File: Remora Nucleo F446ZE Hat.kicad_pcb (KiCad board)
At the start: 2 copper layers, 70 x 133.3 mm, 75 parts, among them J1 NucleoF446ZE CN11 Header, J2 NucleoF446ZE CN12 Header, U10 HT26LS31ARZ, U11 ADuM1201AR, U12 ADuM1201AR, U13 HT26LS31ARZ, U14 ADuM1201AR, U15 ADuM1201AR, U16 ADuM1201AR, U17 ADuM1201AR, U18 ADuM1201AR, U19 ADuM1201AR, U2 TPS5430DDAR, U3 TPS5430DDAR, U4 TPS5430DDAR, U5 ADuM1201AR, U6 ADuM1201AR, U7 ADuM1201AR, U8 ADuM1201AR, U9 HT26LS31ARZ

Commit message: Deleted stale test production files. Fixed up a bug with power isolation. Created some footprints for wire to board connectors although ran out of time to fix a bug where they do no lock in. Fixes to readme
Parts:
- added C10: 100nF, Capacitor_SMD:C_1206_3216Metric_Pad1.33x1.80mm_HandSolder, F.Cu at (-78.6, 41.0)
- added C11: 100nF, Capacitor_SMD:C_1206_3216Metric_Pad1.33x1.80mm_HandSolder, F.Cu at (-78.6, 44.3)
- added C12: 100nF, Capacitor_SMD:C_1206_3216Metric_Pad1.33x1.80mm_HandSolder, F.Cu at (-78.6, 47.7)
- added C13: 100nF, Capacitor_SMD:C_1206_3216Metric_Pad1.33x1.80mm_HandSolder, F.Cu at (-78.6, 51.0)
- added C14: 100nF, Capacitor_SMD:C_1206_3216Metric_Pad1.33x1.80mm_HandSolder, F.Cu at (-95.0, 56.1)
- added C15: 100nF, Capacitor_SMD:C_1206_3216Metric_Pad1.33x1.80mm_HandSolder, F.Cu at (-95.0, 59.5)
- added C16: 100nF, Capacitor_SMD:C_1206_3216Metric_Pad1.33x1.80mm_HandSolder, F.Cu at (-95.0, 62.9)
- added C17: 100nF, Capacitor_SMD:C_1206_3216Metric_Pad1.33x1.80mm_HandSolder, F.Cu at (-95.0, 66.2)
- added C18: 100nF, Capacitor_SMD:C_1206_3216Metric_Pad1.33x1.80mm_HandSolder, F.Cu at (-95.0, 24.7)
- added C19: 100nF, Capacitor_SMD:C_1206_3216Metric_Pad1.33x1.80mm_HandSolder, F.Cu at (-95.0, 28.0)
- added C20: 100nF, Capacitor_SMD:C_1206_3216Metric_Pad1.33x1.80mm_HandSolder, F.Cu at (-95.0, 31.4)
- added C21: 100nF, Capacitor_SMD:C_1206_3216Metric_Pad1.33x1.80mm_HandSolder, F.Cu at (-95.0, 34.7)
- added C22: 100nF, Capacitor_SMD:C_1206_3216Metric_Pad1.33x1.80mm_HandSolder, F.Cu at (-67.7, 32.8)
- added C24: 100nF, Capacitor_SMD:C_1206_3216Metric_Pad1.33x1.80mm_HandSolder, F.Cu at (-112.3, 19.3)
- added C25: 100nF, Capacitor_SMD:C_1206_3216Metric_Pad1.33x1.80mm_HandSolder, F.Cu at (-57.4, 91.9)
- added C26: 100nF, Capacitor_SMD:C_1206_3216Metric_Pad1.33x1.80mm_HandSolder, F.Cu at (-57.4, 95.2)
- added C27: 100nF, Capacitor_SMD:C_1206_3216Metric_Pad1.33x1.80mm_HandSolder, F.Cu at (-36.5, 91.9)
- added C28: 100nF, Capacitor_SMD:C_1206_3216Metric_Pad1.33x1.80mm_HandSolder, F.Cu at (-36.5, 95.2)
- added C29: 100nF, Capacitor_SMD:C_1206_3216Metric_Pad1.33x1.80mm_HandSolder, F.Cu at (-29.5, 44.8)
- added C30: 100nF, Capacitor_SMD:C_1206_3216Metric_Pad1.33x1.80mm_HandSolder, F.Cu at (-29.5, 48.1)
- added C31: 100nF, Capacitor_SMD:C_1206_3216Metric_Pad1.33x1.80mm_HandSolder, F.Cu at (-26.1, 76.6)
- added C32: 100nF, Capacitor_SMD:C_1206_3216Metric_Pad1.33x1.80mm_HandSolder, F.Cu at (-26.1, 79.9)
- added C33: 100nF, Capacitor_SMD:C_1206_3216Metric_Pad1.33x1.80mm_HandSolder, F.Cu at (-72.2, 103.8)
- added C34: 100nF, Capacitor_SMD:C_1206_3216Metric_Pad1.33x1.80mm_HandSolder, F.Cu at (-72.2, 107.2)
- added C35: 100nF, Capacitor_SMD:C_1206_3216Metric_Pad1.33x1.80mm_HandSolder, F.Cu at (-57.4, 107.2)
- added C36: 100nF, Capacitor_SMD:C_1206_3216Metric_Pad1.33x1.80mm_HandSolder, F.Cu at (-57.4, 110.5)
- added C37: 100nF, Capacitor_SMD:C_1206_3216Metric_Pad1.33x1.80mm_HandSolder, F.Cu at (-47.0, 107.2)
- added C38: 100nF, Capacitor_SMD:C_1206_3216Metric_Pad1.33x1.80mm_HandSolder, F.Cu at (-47.0, 110.5)
- added C39: 100nF, Capacitor_SMD:C_1206_3216Metric_Pad1.33x1.80mm_HandSolder, F.Cu at (-47.0, 76.6)
- added C40: 100nF, Capacitor_SMD:C_1206_3216Metric_Pad1.33x1.80mm_HandSolder, F.Cu at (-47.0, 79.9)
- added C41: 100nF, Capacitor_SMD:C_1206_3216Metric_Pad1.33x1.80mm_HandSolder, F.Cu at (-26.1, 107.2)
- added C42: 100nF, Capacitor_SMD:C_1206_3216Metric_Pad1.33x1.80mm_HandSolder, F.Cu at (-26.1, 110.5)
- added C43: 100nF, Capacitor_SMD:C_1206_3216Metric_Pad1.33x1.80mm_HandSolder, F.Cu at (-47.0, 91.9)
- added C44: 100nF, Capacitor_SMD:C_1206_3216Metric_Pad1.33x1.80mm_HandSolder, F.Cu at (-47.0, 95.2)
- added C45: 100nF, Capacitor_SMD:C_1206_3216Metric_Pad1.33x1.80mm_HandSolder, F.Cu at (-36.5, 107.2)
- added C46: 100nF, Capacitor_SMD:C_1206_3216Metric_Pad1.33x1.80mm_HandSolder, F.Cu at (-36.5, 110.5)
- added C47: 100nF, Capacitor_SMD:C_1206_3216Metric_Pad1.33x1.80mm_HandSolder, F.Cu at (-26.1, 91.9)
- added C48: 100nF, Capacitor_SMD:C_1206_3216Metric_Pad1.33x1.80mm_HandSolder, F.Cu at (-26.1, 95.2)
- added C49: 100nF, Capacitor_SMD:C_1206_3216Metric_Pad1.33x1.80mm_HandSolder, F.Cu at (-36.5, 76.6)
- added C50: 100nF, Capacitor_SMD:C_1206_3216Metric_Pad1.33x1.80mm_HandSolder, F.Cu at (-36.5, 79.9)
- added C51: 100nF, Capacitor_SMD:C_1206_3216Metric_Pad1.33x1.80mm_HandSolder, F.Cu at (-57.4, 76.6)
- added C52: 100nF, Capacitor_SMD:C_1206_3216Metric_Pad1.33x1.80mm_HandSolder, F.Cu at (-57.4, 79.9)
- added D8: 3V3LED, Diode_SMD:D_1206_3216Metric_Pad1.42x1.75mm_HandSolder, F.Cu at (-33.2, 24.7)
- added F1: 45mA Resettable Fuse (PRG18BB101MB1RB), Fuse:Fuse_0603_1608Metric_Pad1.05x0.95mm_HandSolder, F.Cu at (-79.4, 96.8)
- added F10: 45mA Resettable Fuse (PRG18BB101MB1RB), Fuse:Fuse_0603_1608Metric_Pad1.05x0.95mm_HandSolder, F.Cu at (-79.4, 69.6)
- added F2: 45mA Resettable Fuse (PRG18BB101MB1RB), Fuse:Fuse_0603_1608Metric_Pad1.05x0.95mm_HandSolder, F.Cu at (-79.4, 56.0)
- added F3: 45mA Resettable Fuse (PRG18BB101MB1RB), Fuse:Fuse_0603_1608Metric_Pad1.05x0.95mm_HandSolder, F.Cu at (-64.6, 56.0)
- added F4: 45mA Resettable Fuse (PRG18BB101MB1RB), Fuse:Fuse_0603_1608Metric_Pad1.05x0.95mm_HandSolder, F.Cu at (-35.0, 56.0)
- added F5: 45mA Resettable Fuse (PRG18BB101MB1RB), Fuse:Fuse_0603_1608Metric_Pad1.05x0.95mm_HandSolder, F.Cu at (-64.6, 83.2)
- added F6: 45mA Resettable Fuse (PRG18BB101MB1RB), Fuse:Fuse_0603_1608Metric_Pad1.05x0.95mm_HandSolder, F.Cu at (-79.4, 83.2)
- added F7: 45mA Resettable Fuse (PRG18BB101MB1RB), Fuse:Fuse_0603_1608Metric_Pad1.05x0.95mm_HandSolder, F.Cu at (-49.8, 56.0)
- added F8: 45mA Resettable Fuse (PRG18BB101MB1RB), Fuse:Fuse_0603_1608Metric_Pad1.05x0.95mm_HandSolder, F.Cu at (-36.7, 37.8)
- added F9: 45mA Resettable Fuse (PRG18BB101MB1RB), Fuse:Fuse_0603_1608Metric_Pad1.05x0.95mm_HandSolder, F.Cu at (-64.6, 69.6)
- added J10: B_STEP_AND_DIR+-, OSTVTerminalBlocks:Conn01x06, F.Cu at (-106.7, 27.1)
- added J11: C_STEP_AND_DIR+-, OSTVTerminalBlocks:Conn01x06, F.Cu at (-106.7, 35.2)
- added J12: DIGITAL_OUTPUTS, OSTVTerminalBlocks:Conn01x12, F.Cu at (-54.4, 27.1)
- added J13: 0-10V Spindle Out, OSTVTerminalBlocks:Conn01x02, F.Cu at (-27.2, 58.8)
- added J14: Digital Inputs, OSTVTerminalBlocks:Conn01x30, F.Cu at (-76.2, 13.6)
- added J3: 5V_SUPPLY, OSTVTerminalBlocks:Conn01x02, F.Cu at (-67.1, 40.6)
- added J4: 5V_AUXOUT, OSTVTerminalBlocks:Conn01x02, F.Cu at (-60.0, 40.6)
- added J5: 24V Power Inlet, OSTVTerminalBlocks:Conn01x02, F.Cu at (-52.9, 40.6)
- added J6: X_STEP_AND_DIR+-, OSTVTerminalBlocks:Conn01x06, F.Cu at (-81.4, 27.1)
- added J7: Y_STEP_AND_DIR+-, OSTVTerminalBlocks:Conn01x06, F.Cu at (-81.4, 35.2)
- added J8: Z_STEP_AND_DIR+-, OSTVTerminalBlocks:Conn01x06, F.Cu at (-106.7, 58.6)
- added J9: A_STEP_AND_DIR+-, OSTVTerminalBlocks:Conn01x06, F.Cu at (-106.7, 66.7)
- added JP1: EXT_5V_SUPPLY_JMP, Jumper:SolderJumper-2_P1.3mm_Open_TrianglePad1.0x1.5mm, F.Cu at (-68.5, 46.4)
- added JP2: EXT_5V_GND_JMP, Jumper:SolderJumper-2_P1.3mm_Open_TrianglePad1.0x1.5mm, F.Cu at (-68.5, 50.0)
- added R17: 100R, Resistor_SMD:R_1206_3216Metric_Pad1.30x1.75mm_HandSolder, F.Cu at (-33.2, 28.0)
- added U10: LTV-817S, Package_SO:SOIC-16_3.9x9.9mm_P1.27mm, F.Cu at (-71.0, 60.6)
- added U11: LTV-817S, Package_SO:SOIC-16_3.9x9.9mm_P1.27mm, F.Cu at (-41.4, 60.6)
- added U12: LTV-817S, Package_SO:SOIC-16_3.9x9.9mm_P1.27mm, F.Cu at (-71.0, 87.8)
- added U13: LTV-817S, Package_SO:SOIC-16_3.9x9.9mm_P1.27mm, F.Cu at (-85.8, 87.8)
- added U14: ADuM1200AR, Package_SO:SOIC-8_3.9x4.9mm_P1.27mm, F.Cu at (-111.1, 74.2)
- added U15: ADuM1200AR, Package_SO:SOIC-8_3.9x4.9mm_P1.27mm, F.Cu at (-111.1, 80.7)
- added U16: HT26LS31ARZ, Package_DIP:SMDIP-4_W9.53mm, F.Cu at (-100.3, 74.1)
- added U17: ADuM1200AR, Package_SO:SOIC-8_3.9x4.9mm_P1.27mm, F.Cu at (-111.1, 42.7)
- added U18: ADuM1200AR, Package_SO:SOIC-8_3.9x4.9mm_P1.27mm, F.Cu at (-111.1, 49.2)
- added U19: HT26LS31ARZ, Package_DIP:SMDIP-4_W9.53mm, F.Cu at (-100.3, 42.6)
- added U20: LTV-817S, Package_SO:SOIC-16_3.9x9.9mm_P1.27mm, F.Cu at (-56.2, 60.6)
- added U21: LTV-817S, Package_SO:SOIC-16_3.9x9.9mm_P1.27mm, F.Cu at (-43.1, 42.4)
- added U22: LTV-817S, Package_SO:SOIC-16_3.9x9.9mm_P1.27mm, F.Cu at (-71.0, 74.2)
- added U23: LTV-817S, Package_SO:SOIC-16_3.9x9.9mm_P1.27mm, F.Cu at (-85.8, 74.2)
- added U26: ADuM1200AR, Package_SO:SOIC-8_3.9x4.9mm_P1.27mm, F.Cu at (-56.2, 87.0)
- added U27: ADuM1200AR, Package_SO:SOIC-8_3.9x4.9mm_P1.27mm, F.Cu at (-35.3, 87.0)
- added U28: ADuM1200AR, Package_SO:SOIC-8_3.9x4.9mm_P1.27mm, F.Cu at (-28.3, 39.9)
- added U29: ADuM1200AR, Package_SO:SOIC-8_3.9x4.9mm_P1.27mm, F.Cu at (-24.8, 71.7)
- added U30: ADuM1200AR, Package_SO:SOIC-8_3.9x4.9mm_P1.27mm, F.Cu at (-71.0, 98.9)
- added U31: ADuM1200AR, Package_SO:SOIC-8_3.9x4.9mm_P1.27mm, F.Cu at (-56.2, 102.2)
- added U32: ADuM1200AR, Package_SO:SOIC-8_3.9x4.9mm_P1.27mm, F.Cu at (-45.7, 102.2)
- added U33: ADuM1200AR, Package_SO:SOIC-8_3.9x4.9mm_P1.27mm, F.Cu at (-45.7, 71.7)
- added U34: ADuM1200AR, Package_SO:SOIC-8_3.9x4.9mm_P1.27mm, F.Cu at (-24.8, 102.2)
- added U35: ADuM1200AR, Package_SO:SOIC-8_3.9x4.9mm_P1.27mm, F.Cu at (-45.7, 87.0)
- added U36: ADuM1200AR, Package_SO:SOIC-8_3.9x4.9mm_P1.27mm, F.Cu at (-35.3, 102.2)
- added U37: ADuM1200AR, Package_SO:SOIC-8_3.9x4.9mm_P1.27mm, F.Cu at (-24.8, 87.0)
- added U38: ADuM1200AR, Package_SO:SOIC-8_3.9x4.9mm_P1.27mm, F.Cu at (-35.3, 71.7)
- added U39: ADuM1200AR, Package_SO:SOIC-8_3.9x4.9mm_P1.27mm, F.Cu at (-56.2, 71.7)
- added U5: ADuM1200AR, Package_SO:SOIC-8_3.9x4.9mm_P1.27mm, F.Cu at (-85.8, 42.7)
- added U6: ADuM1200AR, Package_SO:SOIC-8_3.9x4.9mm_P1.27mm, F.Cu at (-85.8, 49.2)
- added U8: LTV-817S, Package_SO:SOIC-16_3.9x9.9mm_P1.27mm, F.Cu at (-85.8, 101.5)
- added U9: LTV-817S, Package_SO:SOIC-16_3.9x9.9mm_P1.27mm, F.Cu at (-85.8, 60.6)
- U7: renamed from U9; footprint Package_SO:SOIC-16_3.9x9.9mm_P1.27mm -> Package_DIP:SMDIP-4_W9.53mm
- moved U10 271.7 mm to (-74.5, 135.5)
- moved U11 271.7 mm to (-83.5, 146.1)
- moved U12 271.7 mm to (-83.5, 152.7)
- moved U13 271.7 mm to (-74.4, 148.9)
- moved U5 271.7 mm to (-83.5, 119.8)
- moved U6 271.7 mm to (-83.5, 126.4)
- moved U7 271.7 mm to (-83.5, 133.0)
- moved U8 271.7 mm to (-83.5, 139.6)
- moved U7 271.7 mm to (-74.3, 122.4)
- moved C1 179.9 mm to (-101.0, 96.6)
- moved C10 179.9 mm to (-100.9, 125.0)
- moved C11 179.9 mm to (-112.9, 125.0)
- moved C12 179.9 mm to (-100.9, 128.3)
- moved C13 179.9 mm to (-112.9, 131.7)
- moved C14 179.9 mm to (-112.9, 121.7)
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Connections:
- net /Regulators/12V_SENSE renamed /Regulators and Power Management/12V_SENSE
- net /Regulators/3V3_SENSE renamed /Regulators and Power Management/3V3_SENSE
- net /Regulators/5V_SENSE renamed /Regulators and Power Management/5V_SENSE
- J1 pad 14: unconnected-(J1-Pin_14-Pad14) -> MCU_RST
- J1 pad 23: unconnected-(J1-Pin_23-Pad23) -> USR_BTN
- J2 pad 28: unconnected-(J2-Pin_28-Pad28) -> USR_LED
- U7 pad 2: /Stepper_drivers/X_STEP+ -> /X and Y Stepper Drivers/X_STEP+
- U7 pad 3: /Stepper_drivers/X_STEP- -> /X and Y Stepper Drivers/X_STEP-

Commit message: Fixes to screw terminal footprints, updated BOM and included in project folder
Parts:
- added J15: 24V Peripheral, EBWA_02_A:ADAMTECH_EBWA-02-A, F.Cu at (-94.8, 4.50)
- added U40: LTV-817S, Package_SO:SOIC-16_3.9x9.9mm_P1.27mm, F.Cu at (-95.2, -7.75)
- added U42: TL431DBZ, Package_TO_SOT_SMD:SOT-23, F.Cu at (-88.5, -11.2)
- J10, J11, J6, J7, J8, J9: footprint OSTVTerminalBlocks:Conn01x06 -> EBWA_06_A:CONN_EBWA-06-A_ADM
- J12: footprint OSTVTerminalBlocks:Conn01x12 -> EBWA_06_A:CONN_EBWA-12-A_ADM
- J13: value 0-10V Spindle Out -> Spindle Out; footprint OSTVTerminalBlocks:Conn01x02 -> EBWA_02_A:ADAMTECH_EBWA-02-A
- J14: footprint OSTVTerminalBlocks:Conn01x30 -> EBWA_06_A:CONN_EBWA-30-A_ADM
- J5: value 24V Power Inlet -> 24V Logic; footprint OSTVTerminalBlocks:Conn01x02 -> EBWA_02_A:ADAMTECH_EBWA-02-A
- moved J10 192.3 mm to (79.5, -21.0)
- moved J11 192.3 mm to (79.5, -12.8)
- moved J12 192.3 mm to (131.8, -21.0)
- moved J14 192.3 mm to (110.0, -34.5)
- moved J6 192.3 mm to (104.8, -21.0)
- moved J7 192.3 mm to (104.8, -12.8)
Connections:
- C1 pad 1: +12V -> VDD
- C12 pad 2: 5V_GND -> GNDPWR
- C13 pad 2: 5V_GND -> GNDPWR
- C16 pad 2: 5V_GND -> GNDPWR
- C17 pad 2: 5V_GND -> GNDPWR
- C20 pad 2: 5V_GND -> GNDPWR
- C21 pad 2: 5V_GND -> GNDPWR
- C22 pad 2: 5V_GND -> GNDPWR
- C24 pad 2: 5V_GND -> GNDPWR
- C25 pad 2: 5V_GND -> GNDPWR
- C27 pad 2: 5V_GND -> GNDPWR
- C29 pad 2: 5V_GND -> GNDPWR
- C31 pad 2: 5V_GND -> GNDPWR
- C33 pad 2: 5V_GND -> GNDPWR
- C35 pad 2: 5V_GND -> GNDPWR
- C37 pad 2: 5V_GND -> GNDPWR
- C39 pad 2: 5V_GND -> GNDPWR
- C41 pad 2: 5V_GND -> GNDPWR
- C43 pad 2: 5V_GND -> GNDPWR
- C45 pad 2: 5V_GND -> GNDPWR
- C47 pad 2: 5V_GND -> GNDPWR
- C49 pad 2: 5V_GND -> GNDPWR
- C51 pad 2: 5V_GND -> GNDPWR
- C6 pad 1: +12V -> +24V
- D6 pad 1: GNDREF -> GNDPWR
- J10 pad 6: 5V_GND -> GNDPWR
- J11 pad 6: 5V_GND -> GNDPWR
- J12 pad 12: 5V_GND -> GNDPWR
- J13 pad 2: GNDREF -> GNDPWR
- J14 pad 30: 5V_GND -> GNDPWR
- J6 pad 6: 5V_GND -> GNDPWR
- J7 pad 6: 5V_GND -> GNDPWR
- J8 pad 6: 5V_GND -> GNDPWR
- J9 pad 6: 5V_GND -> GNDPWR
- R2 pad 1: +5V -> +5VD
- R3 pad 2: GNDREF -> GNDPWR
- U1 pad 6: +5V -> +5VD
- U10 pad 3: 5V_GND -> GNDPWR
- U11 pad 3: 5V_GND -> GNDPWR
- U12 pad 3: 5V_GND -> GNDPWR
- U13 pad 3: 5V_GND -> GNDPWR
- U14 pad 5: 5V_GND -> GNDPWR
- U15 pad 5: 5V_GND -> GNDPWR
- U17 pad 5: 5V_GND -> GNDPWR
- U18 pad 5: 5V_GND -> GNDPWR
- U2 pad 7: +12V -> VDD
- U20 pad 3: 5V_GND -> GNDPWR
- U21 pad 3: 5V_GND -> GNDPWR
- U22 pad 3: 5V_GND -> GNDPWR
- U23 pad 3: 5V_GND -> GNDPWR
- U26 pad 4: 5V_GND -> GNDPWR
- U27 pad 4: 5V_GND -> GNDPWR
- U28 pad 4: 5V_GND -> GNDPWR
- U29 pad 4: 5V_GND -> GNDPWR
- U30 pad 4: 5V_GND -> GNDPWR
- U31 pad 4: 5V_GND -> GNDPWR
- U32 pad 4: 5V_GND -> GNDPWR
- U33 pad 4: 5V_GND -> GNDPWR
- U34 pad 4: 5V_GND -> GNDPWR
- U35 pad 4: 5V_GND -> GNDPWR
- U36 pad 4: 5V_GND -> GNDPWR
- U37 pad 4: 5V_GND -> GNDPWR
- U38 pad 4: 5V_GND -> GNDPWR
- U39 pad 4: 5V_GND -> GNDPWR
- U4 pad 7: +12V -> +24V
- U5 pad 5: 5V_GND -> GNDPWR
- U6 pad 5: 5V_GND -> GNDPWR
- U8 pad 3: 5V_GND -> GNDPWR
- U9 pad 3: 5V_GND -> GNDPWR

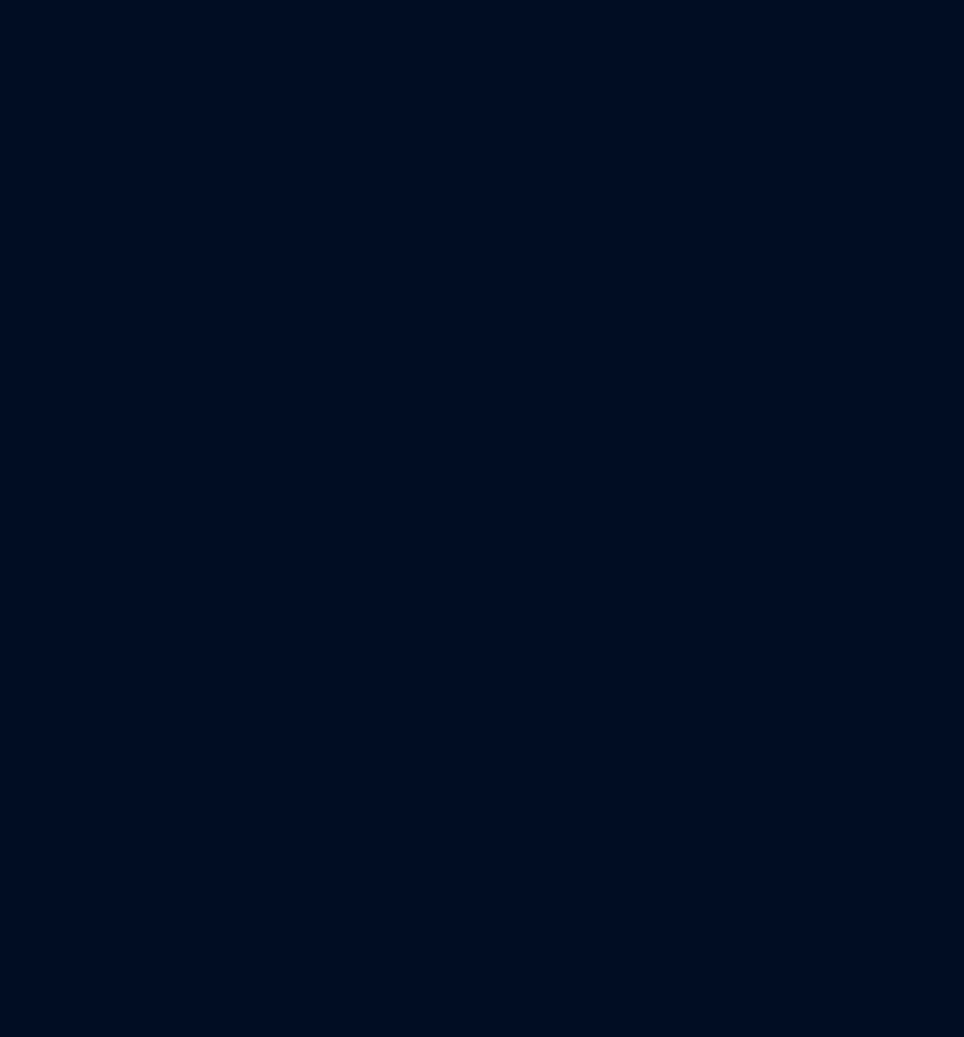
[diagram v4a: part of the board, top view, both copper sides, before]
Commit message: Fixes to bypass caps in micro SD + imported and assigned footprint file
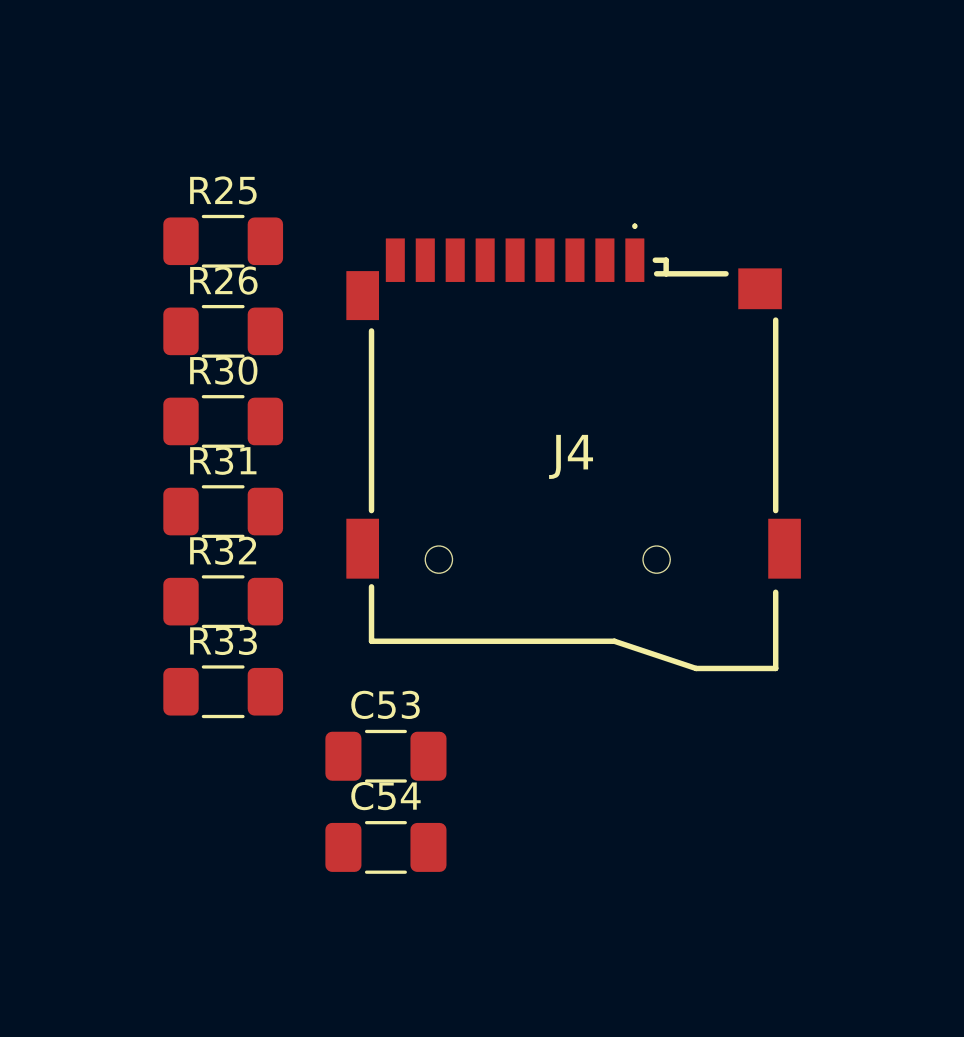
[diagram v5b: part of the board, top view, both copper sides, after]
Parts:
- added C53: 100nF, Capacitor_SMD:C_1206_3216Metric_Pad1.33x1.80mm_HandSolder, F.Cu at (192.9, 61.6)
- added C54: 10uF, Capacitor_SMD:C_1206_3216Metric_Pad1.33x1.80mm_HandSolder, F.Cu at (192.9, 65.0)
- added J4: MSD-1-A, MSD1A Symbols:MSD1A, F.Cu at (199.8, 50.5)
- added R25: 4K7, Resistor_SMD:R_1206_3216Metric_Pad1.30x1.75mm_HandSolder, F.Cu at (186.9, 42.7)
- added R26: 4K7, Resistor_SMD:R_1206_3216Metric_Pad1.30x1.75mm_HandSolder, F.Cu at (186.9, 46.0)
- added R30: 4K7, Resistor_SMD:R_1206_3216Metric_Pad1.30x1.75mm_HandSolder, F.Cu at (186.9, 49.3)
- added R31: 4K7, Resistor_SMD:R_1206_3216Metric_Pad1.30x1.75mm_HandSolder, F.Cu at (186.9, 52.6)
- added R32: 4K7, Resistor_SMD:R_1206_3216Metric_Pad1.30x1.75mm_HandSolder, F.Cu at (186.9, 55.9)
- added R33: 4K7, Resistor_SMD:R_1206_3216Metric_Pad1.30x1.75mm_HandSolder, F.Cu at (186.9, 59.3)
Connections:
- J1 pad 1: unconnected-(J1-Pin_1-Pad1) -> /SDIO_D2
- J1 pad 2: unconnected-(J1-Pin_2-Pad2) -> /SDIO_D3
- J1 pad 3: unconnected-(J1-Pin_3-Pad3) -> /SDIO_CLK
- J1 pad 32: unconnected-(J1-Pin_32-Pad32) -> /SPI1_CS
- J1 pad 4: unconnected-(J1-Pin_4-Pad4) -> /SDIO_CMD
- J2 pad 1: unconnected-(J2-Pin_1-Pad1) -> /SDIO_D1
- J2 pad 17: /WIZ_CS -> unconnected-(J2-Pin_17-Pad17)
- J2 pad 2: unconnected-(J2-Pin_2-Pad2) -> /SDIO_D0

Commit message: Fixed bug with lack of pin header for CN11 and CN12. Addeded RPI header and aligned it, assigned some safe footprints
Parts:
- added J3: UART_TX, EBWA_02_A:ADAMTECH_EBWA-02-A, F.Cu at (176.5, 82.5)
- added R11: 82R, Resistor_SMD:R_1206_3216Metric_Pad1.30x1.75mm_HandSolder, F.Cu at (-4.47, -28.2)
- added R12: 82R, Resistor_SMD:R_1206_3216Metric_Pad1.30x1.75mm_HandSolder, F.Cu at (6.43, -39.1)
- added R13: 82R, Resistor_SMD:R_1206_3216Metric_Pad1.30x1.75mm_HandSolder, F.Cu at (-4.47, -22.9)
- added R14: 82R, Resistor_SMD:R_1206_3216Metric_Pad1.30x1.75mm_HandSolder, F.Cu at (3.48, -22.9)
- added R15: 82R, Resistor_SMD:R_1206_3216Metric_Pad1.30x1.75mm_HandSolder, F.Cu at (-12.4, -23.9)
- added R16: 82R, Resistor_SMD:R_1206_3216Metric_Pad1.30x1.75mm_HandSolder, F.Cu at (3.48, -33.5)
- added R19: 10K, Resistor_SMD:R_1206_3216Metric_Pad1.30x1.75mm_HandSolder, F.Cu at (-12.4, -18.6)
- added R20: 82R, Resistor_SMD:R_1206_3216Metric_Pad1.30x1.75mm_HandSolder, F.Cu at (3.48, -28.2)
- added R21: 82R, Resistor_SMD:R_1206_3216Metric_Pad1.30x1.75mm_HandSolder, F.Cu at (6.43, -44.5)
- added R22: 82R, Resistor_SMD:R_1206_3216Metric_Pad1.30x1.75mm_HandSolder, F.Cu at (-12.4, -29.2)
- added R23: 82R, Resistor_SMD:R_1206_3216Metric_Pad1.30x1.75mm_HandSolder, F.Cu at (-4.47, -33.5)
- added R24: 10K, Resistor_SMD:R_1206_3216Metric_Pad1.30x1.75mm_HandSolder, F.Cu at (-12.4, -44.5)
- added R27: 82R, Resistor_SMD:R_1206_3216Metric_Pad1.30x1.75mm_HandSolder, F.Cu at (-12.4, -41.1)
- added R28: 10K, Resistor_SMD:R_1206_3216Metric_Pad1.30x1.75mm_HandSolder, F.Cu at (-12.4, -37.8)
- added R29: 30K, Resistor_SMD:R_1206_3216Metric_Pad1.30x1.75mm_HandSolder, F.Cu at (-12.4, -34.5)
- added RP1: Raspberry_Pi_2_3, RPI3FootPrint:raspberrypi_2_3, B.Cu at (176.5, 118.1)
- D8: value 3V3LED -> USR_LED
- J1, J2: footprint Connector_PinHeader_2.54mm:PinHeader_2x31_P2.54mm_Vertical -> Connector_PinHeader_2.54mm:PinHeader_2x35_P2.54mm_Vertical
- moved R1 299.6 mm to (177.8, 74.7), turned to 90 degrees
- moved D1 296.8 mm to (175.3, 74.6), turned to 90 degrees
- moved J8 175.3 mm to (49.8, -20.3)
- moved J9 174.4 mm to (49.8, -10.2)
- moved R17 142.4 mm to (109.2, 30.2), turned to 90 degrees
- moved D8 139.9 mm to (106.7, 30.3), turned to 90 degrees
- moved J4 31.4 mm to (171.2, 37.4), turned to 180 degrees
- moved U1 18.8 mm to (145.7, 55.4)
- moved C53 16.1 mm to (196.3, 45.9)
- moved R30 16.1 mm to (190.3, 33.6)
- moved R32 16.1 mm to (190.3, 40.2)
- moved R33 16.1 mm to (190.3, 43.6)
- moved R25 16.1 mm to (190.3, 27.0)
- moved R26 16.1 mm to (190.3, 30.3)
- moved C54 16.1 mm to (196.3, 49.3)
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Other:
- board size 70 x 133.3 mm -> 80.2 x 133.3 mm

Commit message: corrected hole spacing for Nucleo board. Double checked some of the standoff spacing and made some correction to pin header insulation heights and standoff heights too.
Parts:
- moved J12 223.3 mm to (-91.2, -33.7)
- moved J14 223.3 mm to (-112.9, -47.2)
- moved J6 223.3 mm to (-118.1, -33.7)
- moved J7 223.3 mm to (-118.1, -25.5)
- moved J8 223.3 mm to (-173.1, -33.0)
- moved J9 223.3 mm to (-173.1, -22.9)
- moved J10 223.3 mm to (-143.4, -33.7)
- moved J11 223.3 mm to (-143.4, -25.5)
- moved R11 111.1 mm to (-93.6, 38.1)
- moved R13 111.1 mm to (-93.6, 43.4)
- moved R14 111.1 mm to (-85.7, 43.4)
- moved R15 111.1 mm to (-101.6, 42.4)
- moved R16 111.1 mm to (-85.7, 32.8)
- moved R19 111.1 mm to (-101.6, 47.7)
- moved R20 111.1 mm to (-85.7, 38.1)
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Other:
- board text added: "Raspberry Pi"
- board text added: "Wiznet 5500"
